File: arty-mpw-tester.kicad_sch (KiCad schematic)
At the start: 107 parts, among them J10 61300211121, J11 61300211121, J12 61300211121, J14 61300311121, J15 61300311121, J18 61300411121, J19 61300711121, J20 61300411121, J3 arty_chipKIT_connector, J4 61300211121, J5 61300311121, J6 61300211121, J7 61300211121, J8 61300211121, J9 61300211121, Q1 DTC014TEBTL, SW1 JS202011JCQN, SW3 JS202011JCQN, U1 PAC1954T-E/4MX, U3 PAC1954T-E/4MX, U4 MAX811REUS+T, U5 NTS0102DP, U6 MCP4661-103E/ML, U7 Caravel_breakout_PCB_flexypin, U8 W25Q32FVSS, U9 MIC2211-AAYML-TR, Y2 ECS-2520MVLC-100-BN-TR

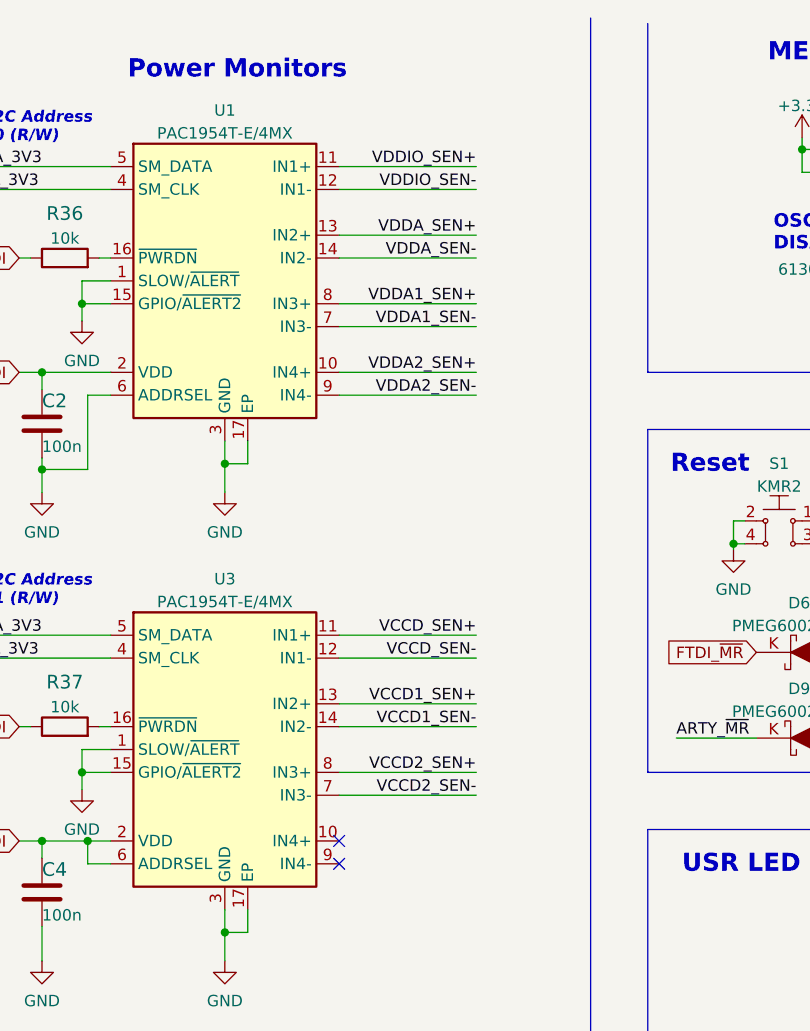
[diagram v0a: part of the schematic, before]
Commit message: Finished initial routing. Corrected switch footprint
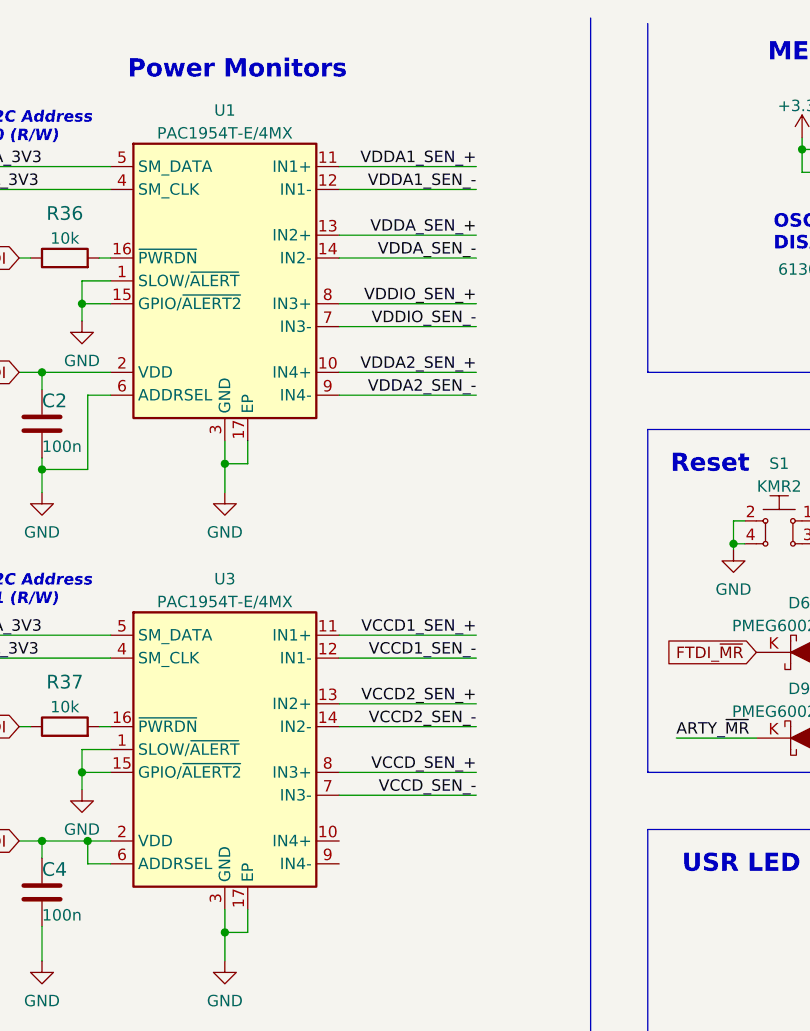
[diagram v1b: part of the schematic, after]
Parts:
- NT1, NT10, NT11, NT12, NT13, NT14, NT2, NT3, NT4, NT5, NT6, NT7, NT8, NT9: footprint antmicro-footprints:NetTie-2_SMD_Pad0.127mm -> NetTie-2_SMD_Pad0.15mm
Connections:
- net VCCD1_SEN+ is gone; now on net VCCD2_SEN_+: U3.13 (IN2+)
- net VCCD1_SEN- is gone; now on net VCCD2_SEN_-: U3.14 (IN2-)
- net VCCD2_SEN+ is gone; now on net VCCD_SEN_+: U3.8 (IN3+)
- net VCCD2_SEN- is gone; now on net VCCD_SEN_-: U3.7 (IN3-)
- net VCCD_SEN+ is gone; now on net VCCD1_SEN_+: U3.11 (IN1+)
- net VCCD_SEN- is gone; now on net VCCD1_SEN_-: U3.12 (IN1-)
- net VDDA1_SEN+ is gone; now on net VDDIO_SEN_+: U1.8 (IN3+)
- net VDDA1_SEN- is gone; now on net VDDIO_SEN_-: U1.7 (IN3-)
- net VDDA2_SEN+ is gone; now on net VDDA2_SEN_+: U1.10 (IN4+)
- net VDDA2_SEN- is gone; now on net VDDA2_SEN_-: U1.9 (IN4-)
- net VDDA_SEN+ is gone; now on net VDDA_SEN_+: U1.13 (IN2+)
- net VDDA_SEN- is gone; now on net VDDA_SEN_-: U1.14 (IN2-)
- net VDDIO_SEN+ is gone; now on net VDDA1_SEN_+: U1.11 (IN1+)
- net VDDIO_SEN- is gone; now on net VDDA1_SEN_-: U1.12 (IN1-)
- no-connect marks 13 -> 11

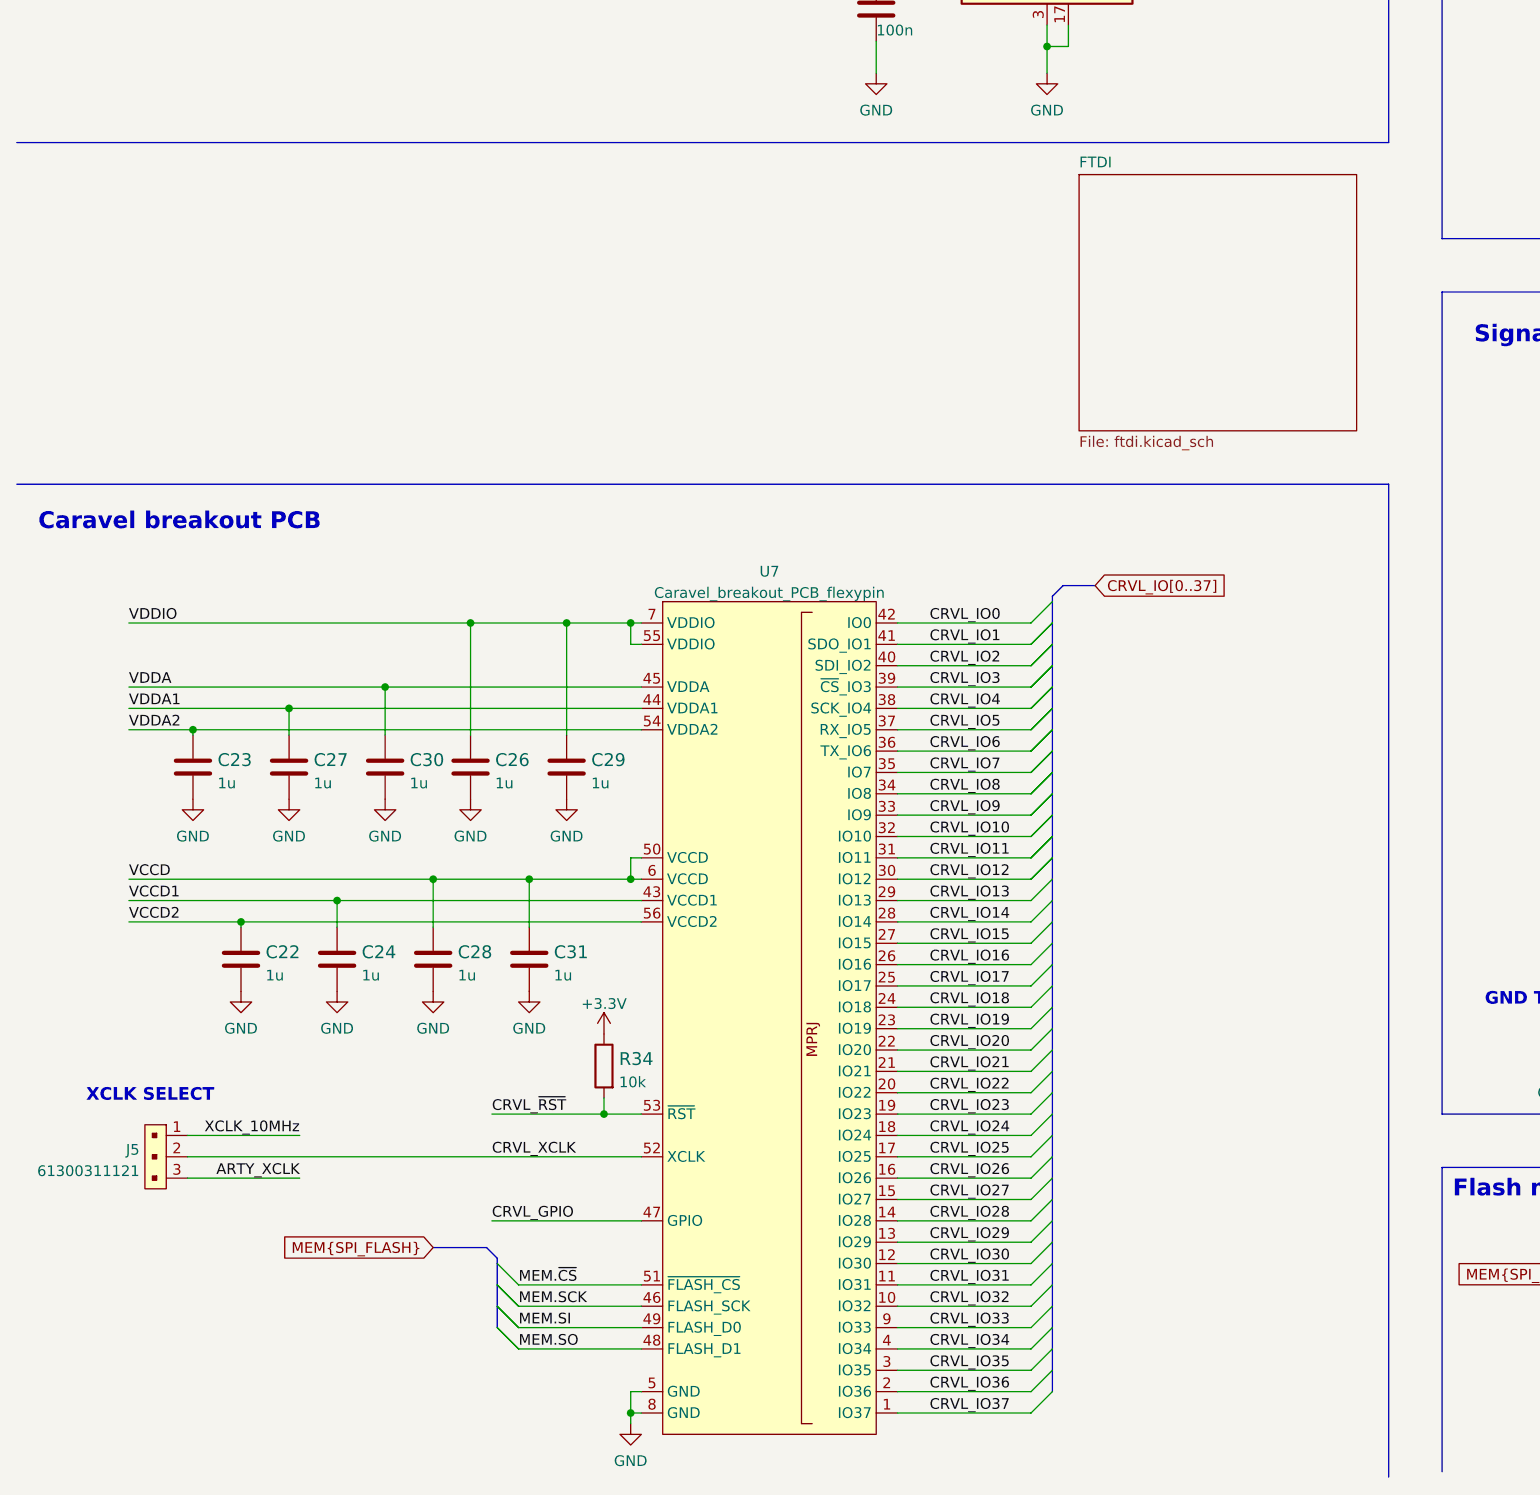
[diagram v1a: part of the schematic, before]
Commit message: Optimized some paths. orrected power plane under USB tracks
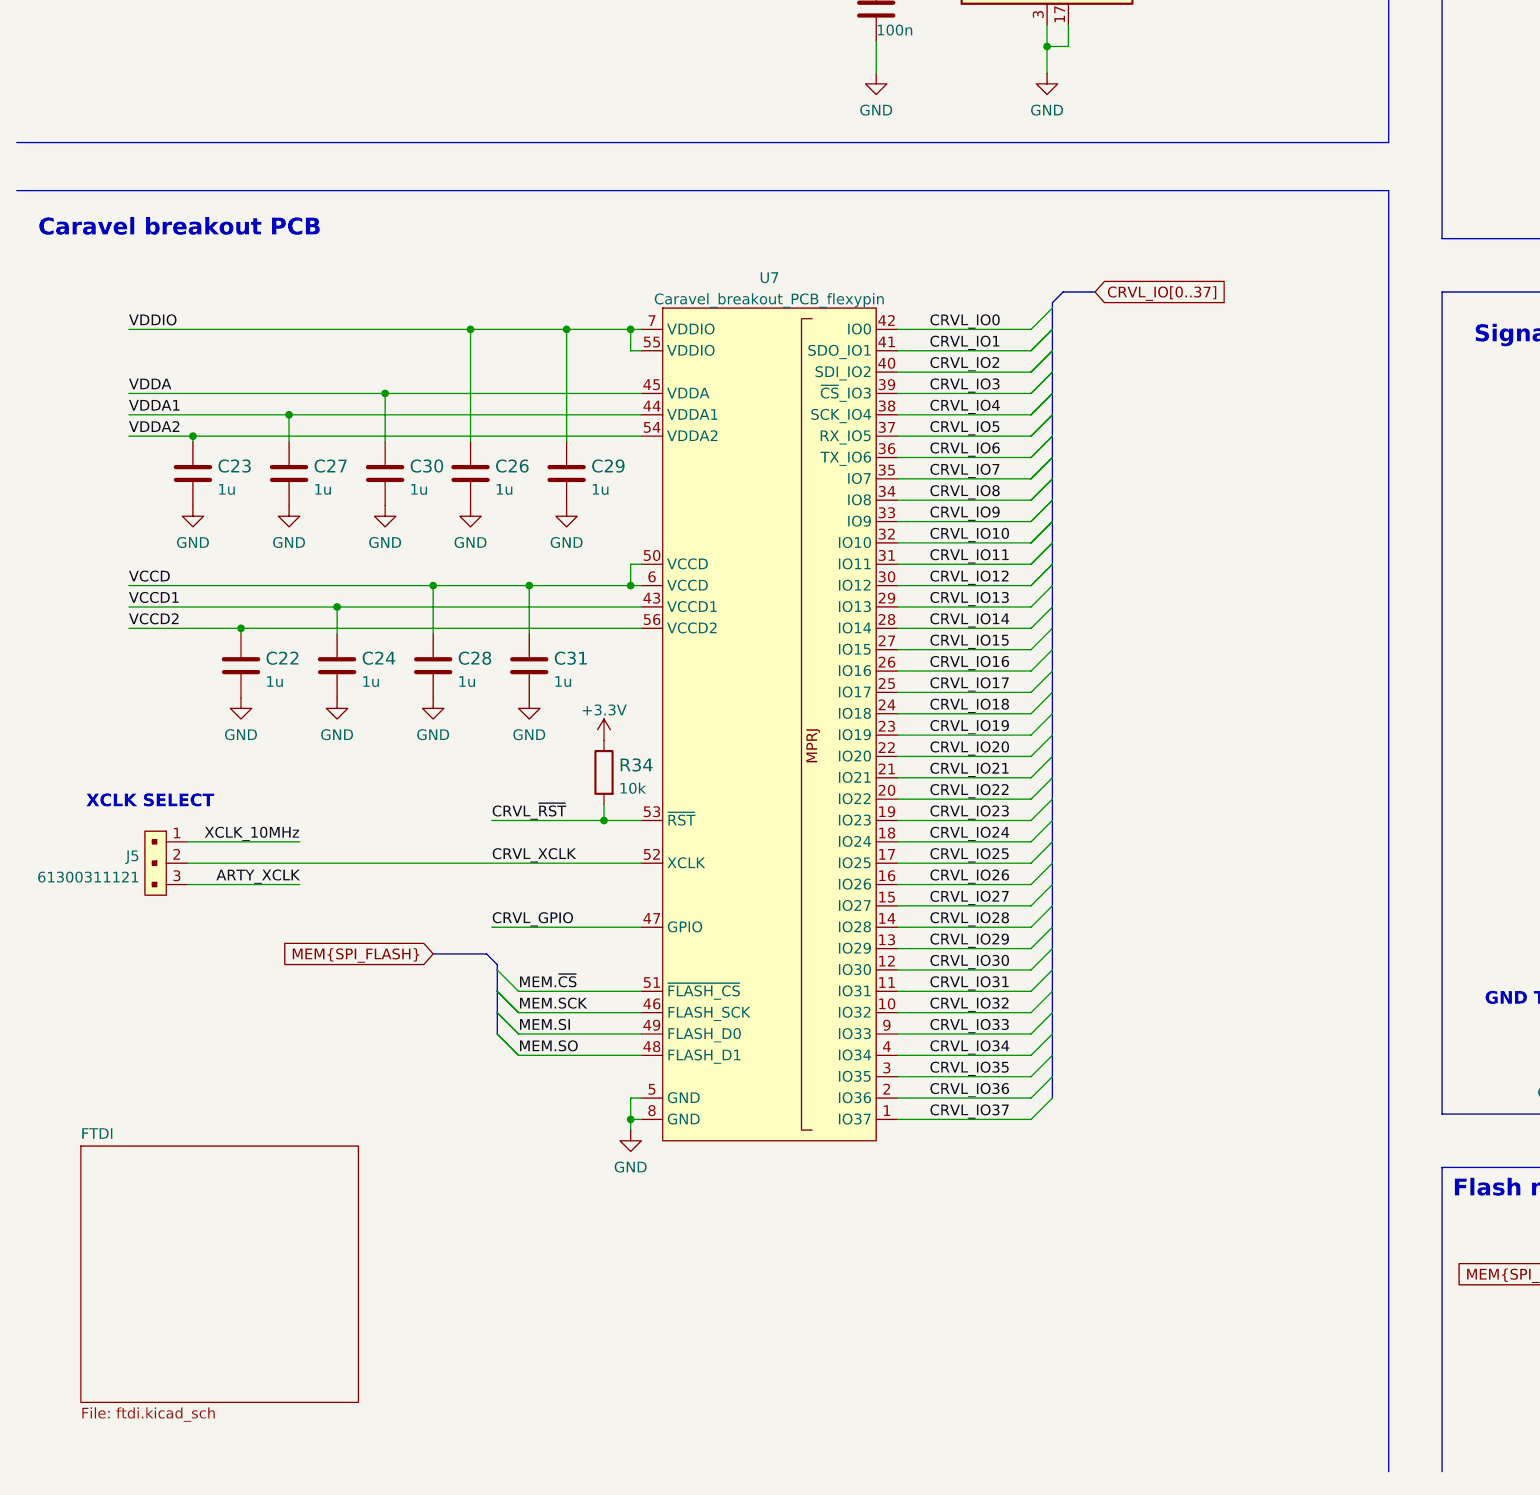
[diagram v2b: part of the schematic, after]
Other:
- moved on the sheet: C22, C23, C24, C26, C27, C28, C29, C30, C31, J5, R34, U7

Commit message: Added slight visual adjustments
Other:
- note added: "Caravel Power Monitors"
- note added: "FTDI Module"
- note removed: "Power Monitors"
- moved on the sheet: C20, C22, C23, C24, C26, C27, C28, C29, C30, C31, D6, D9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

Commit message: Loclib
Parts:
- NT1, NT10, NT11, NT12, NT13, NT14, NT2, NT3, NT4, NT5, NT6, NT7, NT8, NT9: footprint NetTie-2_SMD_Pad0.15mm -> arty-mpw-tester-footprints:NetTie-2_SMD_Pad0.15mm; symbol antmicroShuntsJumpers:NetTie_2 -> arty-mpw-tester:NetTie_2
- R1, R10, R38, R39, R40, R41, R9: footprint antmicro-footprints:1206-res -> arty-mpw-tester-footprints:1206-res; symbol antmicroResistorsmisc:R_0R01_1206 -> arty-mpw-tester:R_0R01_1206
- U1, U3: footprint antmicro-footprints:VQFN-16-1EP_3x3mm_P0.5mm_EP1.1x1.1mm -> arty-mpw-tester-footprints:VQFN-16-1EP_3x3mm_P0.5mm_EP1.1x1.1mm; symbol antmicroMicrocontrollers:PAC1954T-E/4MX -> arty-mpw-tester:PAC1954T-E/4MX
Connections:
- net ARTY_MEM_CS: no longer J3.25 (SS)
- net ARTY_MEM_MISO: no longer J3.28 (MISO)
- net ARTY_MEM_MOSI: no longer J3.29 (MOSI)
- net ARTY_MEM_SCK: no longer J3.27 (SCK)
- net EP: no longer J3.26 (GND)

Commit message: Fix broken symbol after loclib
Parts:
- removed unit 3 of J3
- added unit 3 of J3
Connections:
- net ARTY_MEM_CS: now also J3.25 (SS)
- net ARTY_MEM_MISO: now also J3.28 (MISO)
- net ARTY_MEM_MOSI: now also J3.29 (MOSI)
- net ARTY_MEM_SCK: now also J3.27 (SCK)
- net EP: now also J3.26 (GND)
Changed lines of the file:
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@@
     (comment 2 "Antmicro Ltd.")
   )
-  (bus_alias "SPI" (members "~{CS}" "MISO" "MOSI" "SCK"))
   (bus_alias "SPI_FLASH" (members "~{CS}" "SCK" "SI" "SO" "~{WP}" "~{HOLD}"))
+  (bus_alias "SPI" (members "~{CS}" "MISO" "MOSI" "SCK"))
   (junction (at 313.69 42.545) (diameter 0) (color 0 0 0 0)
   )
@@
     (pin "1")
   )
-  (symbol (lib_name "arty_chipKIT_connector_1") (lib_id "arty-mpw-tester:arty_chipKIT_connector") (at 367.03 220.98 0) (unit 3)
-    (in_bom yes) (on_board yes) (fields_autoplaced)
-    (property "Reference" "J3" (id 0) (at 367.665 212.251 0))
-    (property "Value" "arty_chipKIT_connector" (id 1) (at 367.665 214.7879 0))
-    (property "Footprint" "arty-mpw-tester-footprints:ARTY_A7_SHIELD" (id 2) (at 367.03 250.19 0)
-      (effects (font (size 1.27 1.27)) hide)
-    )
-    (property "Datasheet" "" (id 3) (at 363.22 222.25 0)
-      (effects (font (size 1.27 1.27)) hide)
-    )
-    (property "Manufacturer" "TE Conectivity" (id 4) (at 367.03 234.95 0)
-      (effects (font (size 1.27 1.27)) hide)
-    )
-    (property "MPN" "9-146281-0" (id 5) (at 367.03 242.57 0)
-      (effects (font (size 1.27 1.27)) hide)
-    )
-    (property "Manufacturer1" "TE Conectivity" (id 6) (at 367.03 240.03 0)
-      (effects (font (size 1.27 1.27)) hide)
-    )
-    (property "MPN1" "2-826629-0" (id 7) (at 367.03 237.49 0)
-      (effects (font (size 1.27 1.27)) hide)
-    )
-    (property "Manufacturer2" "HARWIN" (id 8) (at 367.03 245.11 0)
-      (effects (font (size 1.27 1.27)) hide)
-    )
-    (property "MPN2" "M20-7830346" (id 9) (at 367.03 247.65 0)
-      (effects (font (size 1.27 1.27)) hide)
-    )
-  )
   (symbol (lib_id "arty-mpw-tester:C_100n_0603") (at 287.02 270.51 0) (unit 1)
     (in_bom yes) (on_board yes) (fields_autoplaced)
@@
     (pin "2")
   )
+  (symbol (lib_id "antmicroModules:arty_chipKIT_connector") (at 367.03 220.98 0) (unit 3)
+    (in_bom yes) (on_board yes) (fields_autoplaced)
+    (property "Reference" "J3" (id 0) (at 367.665 210.82 0))
+    (property "Value" "arty_chipKIT_connector" (id 1) (at 367.665 213.36 0))
+    (property "Footprint" "antmicro-footprints:ARTY_A7_SHIELD" (id 2) (at 367.03 250.19 0)
+      (effects (font (size 1.27 1.27)) hide)
+    )
+    (property "Datasheet" "" (id 3) (at 363.22 222.25 0)
+      (effects (font (size 1.27 1.27)) hide)
+    )
+    (property "Manufacturer" "TE Conectivity" (id 4) (at 367.03 234.95 0)
+      (effects (font (size 1.27 1.27)) hide)
+    )
+    (property "MPN" "9-146281-0" (id 5) (at 367.03 242.57 0)
+      (effects (font (size 1.27 1.27)) hide)
+    )
+    (property "Manufacturer1" "TE Conectivity" (id 6) (at 367.03 240.03 0)
+      (effects (font (size 1.27 1.27)) hide)
+    )
+    (property "MPN1" "2-826629-0" (id 7) (at 367.03 237.49 0)
+      (effects (font (size 1.27 1.27)) hide)
+    )
+    (property "Manufacturer2" "HARWIN" (id 8) (at 367.03 245.11 0)
+      (effects (font (size 1.27 1.27)) hide)
+    )
+    (property "MPN2" "M20-7830346" (id 9) (at 367.03 260.35 0)
+      (effects (font (size 1.27 1.27)) hide)
+    )
+    (pin "1")
+    (pin "10")
+    (pin "11")
+    (pin "12")
+    (pin "13")
+    (pin "14")
+    (pin "15")
+    (pin "16")
+    (pin "17")
+    (pin "18")
+    (pin "19")
+    (pin "2")
+    (pin "20")
+    (pin "21")
+    (pin "22")
+    (pin "23")
+    (pin "24")
+    (pin "3")
+    (pin "4")
+    (pin "5")
+    (pin "6")
+    (pin "7")
+    (pin "8")
+    (pin "9")
+    (pin "31")
+    (pin "32")
+    (pin "33")
+    (pin "34")
+    (pin "35")
+    (pin "36")
+    (pin "37")
+    (pin "38")
+    (pin "39")
+    (pin "40")
+    (pin "41")
+    (pin "42")
+    (pin "43")
+    (pin "44")
+    (pin "45")
+    (pin "46")
+    (pin "47")
+    (pin "48")
+    (pin "49")
+    (pin "50")
+    (pin "51")
+    (pin "52")
+    (pin "53")
+    (pin "54")
+    (pin "55")
+    (pin "56")
+    (pin "57")
+    (pin "58")
+    (pin "59")
+    (pin "60")
+    (pin "61")
+    (pin "62")
+    (pin "63")
+    (pin "64")
+    (pin "25")
+    (pin "26")
+    (pin "27")
+    (pin "28")
+    (pin "29")
+    (pin "30")
+  )
   (symbol (lib_id "arty-mpw-tester:RCW-0C") (at 196.215 231.775 180) (unit 1)
     (in_bom yes) (on_board yes) (fields_autoplaced)
@@
       (reference "J3") (unit 2) (value "arty_chipKIT_connector") (footprint "arty-mpw-tester-footprints:ARTY_A7_SHIELD")
     )
-    (path "/612b92e0-3a44-444b-8188-38feb66dfe96"
-      (reference "J3") (unit 3) (value "arty_chipKIT_connector") (footprint "arty-mpw-tester-footprints:ARTY_A7_SHIELD")
+    (path "/cd4b7f9b-3970-4161-b937-ec055ff66715"
+      (reference "J3") (unit 3) (value "arty_chipKIT_connector") (footprint "antmicro-footprints:ARTY_A7_SHIELD")
     )
     (path "/6f67b8f8-bfb8-4822-b7cf-608f56e7f0fc"
